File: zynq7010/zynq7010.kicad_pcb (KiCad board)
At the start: 2 copper layers, 50 x 50 mm, 131 parts, among them J1 Conn_02x15_Odd_Even, U1 xc7z010clg400, U2 TPS563200, U3 TPS563200, U4 TPS563200, U5 TPS563200, U6 MT41K256M16HA, U7 MT41K256M16HA

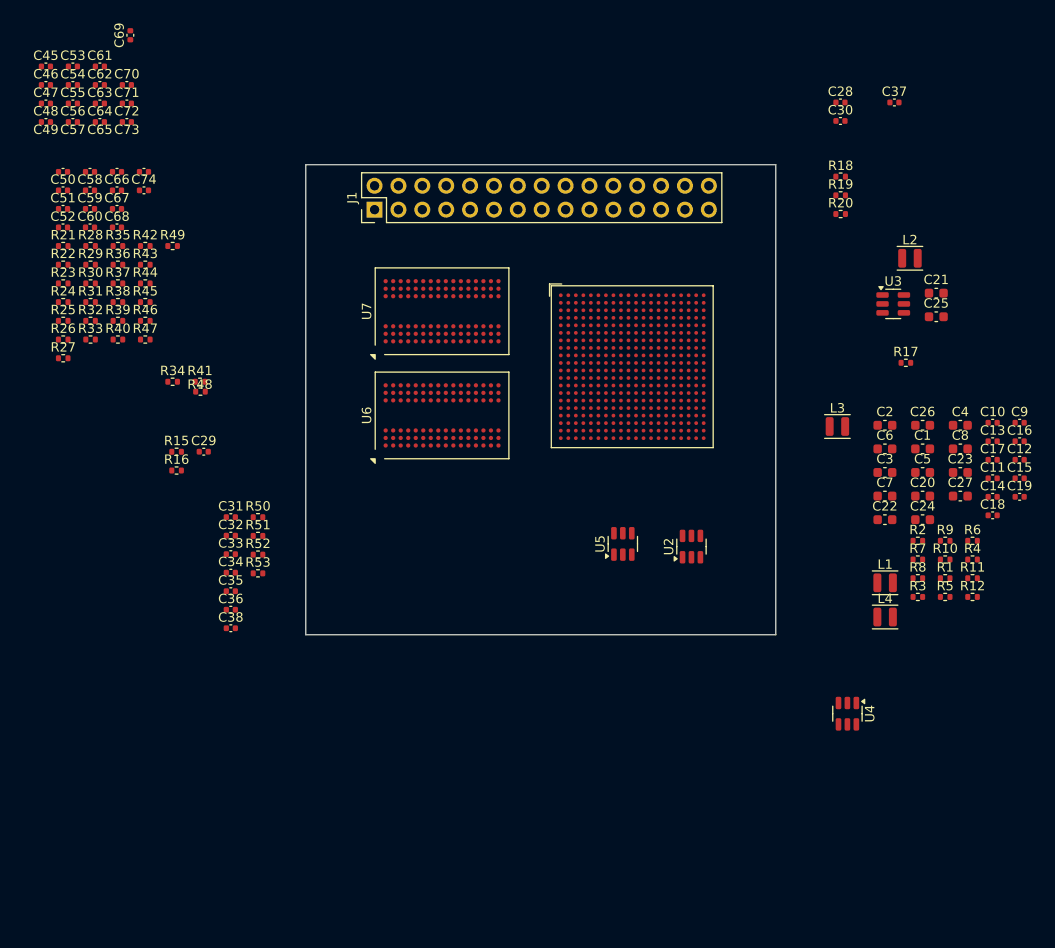
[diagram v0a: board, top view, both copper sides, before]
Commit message: finish dcdc and vtt sch, later do crystal and sd card
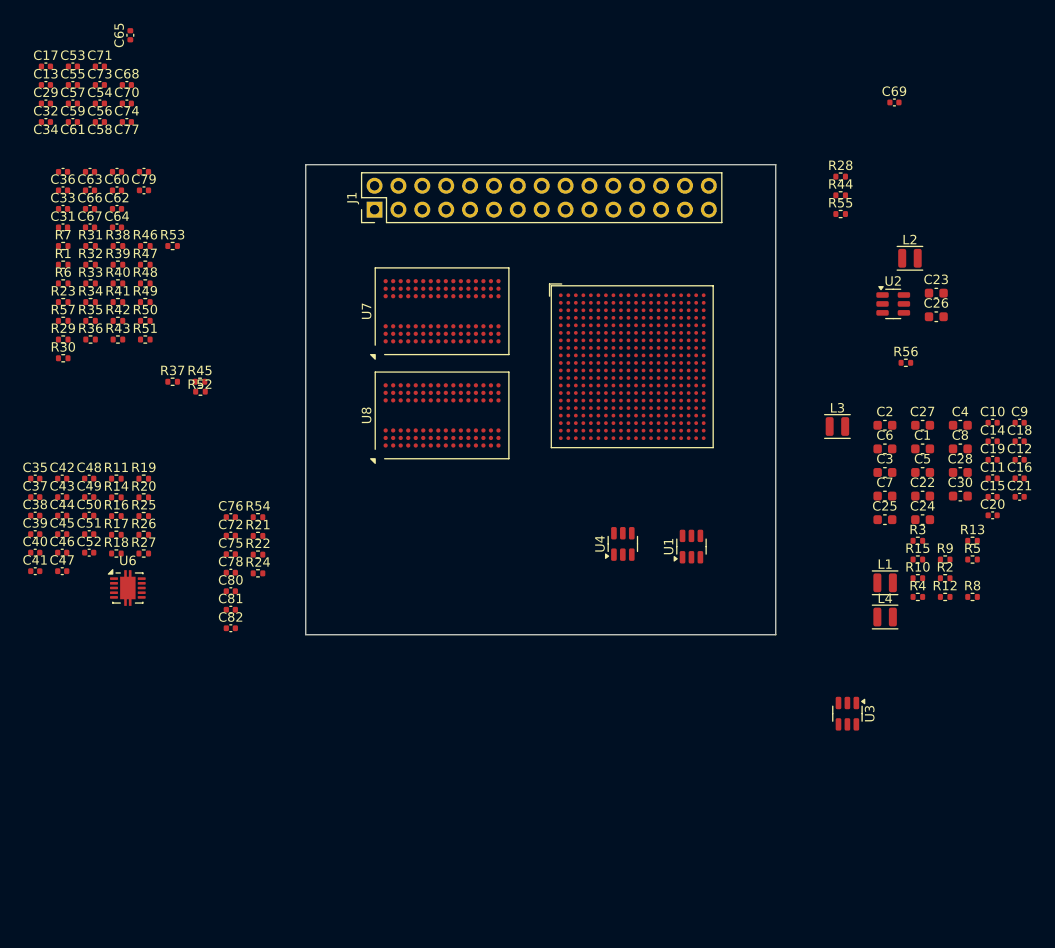
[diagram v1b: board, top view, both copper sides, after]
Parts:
- removed the C28 at (152.9, 49.7)
- removed the C29 at (85.1, 86.9)
- removed the C30 at (152.9, 51.7)
- removed the R15 at (82.2, 86.9)
- removed the R9 at (164.0, 96.3)
- added C35: 4.7uF, Capacitor_SMD:C_0402_1005Metric, F.Cu at (67.2, 89.7)
- added C37: 10uF, Capacitor_SMD:C_0402_1005Metric, F.Cu at (67.2, 91.7)
- added C38: 10uF, Capacitor_SMD:C_0402_1005Metric, F.Cu at (67.2, 93.7)
- added C39: 10uF, Capacitor_SMD:C_0402_1005Metric, F.Cu at (67.2, 95.6)
- added C40: 10uF, Capacitor_SMD:C_0402_1005Metric, F.Cu at (67.2, 97.6)
- added C41: 10uF, Capacitor_SMD:C_0402_1005Metric, F.Cu at (67.2, 99.6)
- added C42: 47uF, Capacitor_SMD:C_0402_1005Metric, F.Cu at (70.1, 89.7)
- added C43: 47uF, Capacitor_SMD:C_0402_1005Metric, F.Cu at (70.1, 91.7)
- added C44: 100nF, Capacitor_SMD:C_0402_1005Metric, F.Cu at (70.1, 93.7)
- added C45: 0.1uF, Capacitor_SMD:C_0402_1005Metric, F.Cu at (70.1, 95.6)
- added C46: 100nF, Capacitor_SMD:C_0402_1005Metric, F.Cu at (70.1, 97.6)
- added C47: 0.1uF, Capacitor_SMD:C_0402_1005Metric, F.Cu at (70.1, 99.6)
- added C48: 10uF, Capacitor_SMD:C_0402_1005Metric, F.Cu at (72.9, 89.7)
- added C49: 0.1uF, Capacitor_SMD:C_0402_1005Metric, F.Cu at (72.9, 91.7)
- added C50: 0.1uF, Capacitor_SMD:C_0402_1005Metric, F.Cu at (72.9, 93.7)
- added C51: 10uF, Capacitor_SMD:C_0402_1005Metric, F.Cu at (72.9, 95.6)
- added C52: 10uF, Capacitor_SMD:C_0402_1005Metric, F.Cu at (72.9, 97.6)
- added R14: 10k, Resistor_SMD:R_0402_1005Metric, F.Cu at (75.8, 91.7)
- added R17: 3.3k, Resistor_SMD:R_0402_1005Metric, F.Cu at (75.8, 95.7)
- added R18: 10k, Resistor_SMD:R_0402_1005Metric, F.Cu at (75.8, 97.7)
- added R19: 10k, Resistor_SMD:R_0402_1005Metric, F.Cu at (78.7, 89.7)
- added R20: 3k, Resistor_SMD:R_0402_1005Metric, F.Cu at (78.7, 91.7)
- added R25: 10k, Resistor_SMD:R_0402_1005Metric, F.Cu at (78.7, 93.7)
- added R26: 10k, Resistor_SMD:R_0402_1005Metric, F.Cu at (78.7, 95.7)
- added R27: 10k, Resistor_SMD:R_0402_1005Metric, F.Cu at (78.7, 97.7)
- added U6: TPS51200DRC, Package_SON:VSON-10-1EP_3x3mm_P0.5mm_EP1.65x2.4mm, F.Cu at (77.1, 101.4)
- R11: value 13.7k -> 7.5k
- R12: renamed from R5; value 13.7k -> 3k
- R15: renamed from R7; value 13.7k -> 10k
- R16: value 1k -> 2k
- moved R11 91.7 mm to (75.8, 89.7)
- moved R16 8.03 mm to (75.8, 93.7)
- renumbered C46 to C13, C13 to C14, C14 to C15, C15 to C16, C45 to C17, C16 to C18, C17 to C19, C18 to C20, C19 to C21, C20 to C22, C21 to C23, C22 to C25, C25 to C26, C26 to C27, C23 to C28, C47 to C29, C27 to C30, C52 to C31, C48 to C32, C51 to C33, C49 to C34, C50 to C36, C63 to C54, C54 to C55, C64 to C56, C55 to C57, C65 to C58, C56 to C59, C66 to C60, C57 to C61, C67 to C62, C58 to C63, C68 to C64, C69 to C65, C59 to C66, C60 to C67, C70 to C68, C37 to C69, C71 to C70, C61 to C71, C32 to C72, C62 to C73, C72 to C74, C33 to C75, C31 to C76, C73 to C77, C34 to C78, C74 to C79, C35 to C80, C36 to C81, C38 to C82, R22 to R1, R8 to R10, R6 to R13, R1 to R2, R51 to R21, R52 to R22, R24 to R23, R53 to R24, R18 to R28, R26 to R29, R2 to R3, R27 to R30, R28 to R31, R29 to R32, R30 to R33, R31 to R34, R32 to R35, R33 to R36, R34 to R37, R35 to R38, R36 to R39, R3 to R4, R37 to R40, R38 to R41, R39 to R42, R40 to R43, R19 to R44, R41 to R45, R42 to R46, R43 to R47, R44 to R48, R45 to R49, R4 to R5, R46 to R50, R47 to R51, R48 to R52, R49 to R53, R50 to R54, R20 to R55, R17 to R56, R25 to R57, R23 to R6, R21 to R7, R12 to R8, R10 to R9, U2 to U1, U3 to U2, U4 to U3, U5 to U4, U1 to U5, U6 to U8
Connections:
- R10 pad 1: Net-(U3-VFB) -> Net-(U2-VFB)
- R11 pad 1: +3V3 -> Net-(U3-VFB)
- R11 pad 2: Net-(U5-VFB) -> Net-(R11-Pad2)
- R15 pad 1: +1V8 -> Net-(U2-VFB)
- R15 pad 2: Net-(U3-VFB) -> Net-(R15-Pad2)
- R16 pad 1: GND -> Net-(R11-Pad2)
- R16 pad 2: VREF_DDR -> +1V5
- R8 pad 1: Net-(U5-VFB) -> Net-(U4-VFB)
- R9 pad 1: Net-(U4-VFB) -> Net-(U3-VFB)
- U2 pad 4: Net-(U3-VFB) -> Net-(U2-VFB)
- U3 pad 4: Net-(U4-VFB) -> Net-(U3-VFB)
- U4 pad 4: Net-(U5-VFB) -> Net-(U4-VFB)

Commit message: done routing between two ddr3
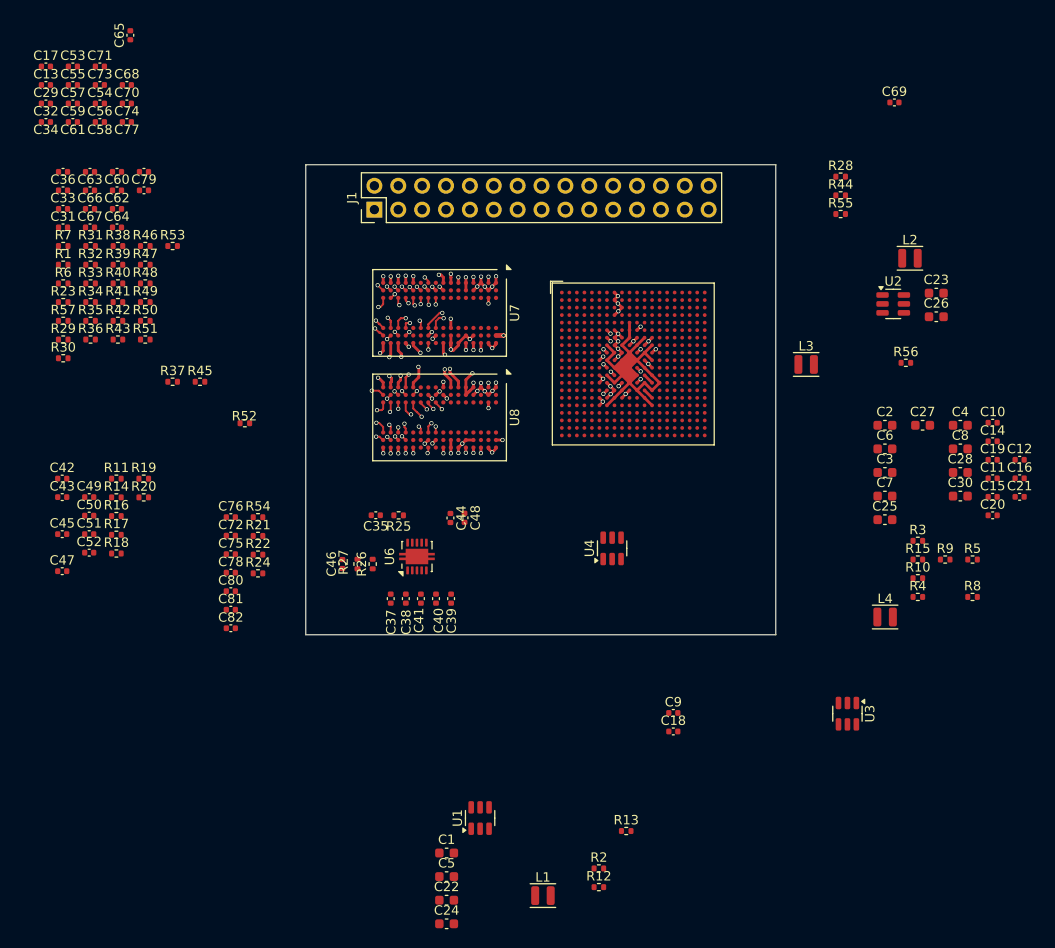
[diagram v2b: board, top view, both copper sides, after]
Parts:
- moved C1 66.4 mm to (111.0, 129.6)
- moved C24 66.4 mm to (111.0, 137.1)
- moved C5 66.4 mm to (111.0, 132.1)
- moved C22 66.4 mm to (111.0, 134.6)
- moved L1 49.3 mm to (121.2, 134.1)
- moved R12 48.1 mm to (127.2, 133.2)
- moved R2 48.1 mm to (127.2, 131.2)
- moved R13 48.1 mm to (130.1, 127.2)
- moved C18 48.1 mm to (135.1, 116.6)
- moved C9 48.1 mm to (135.1, 114.7)
- moved C39 44.8 mm to (111.4, 102.5), turned to -90 degrees
- moved C40 42.9 mm to (109.8, 102.5), turned to -90 degrees
- moved C44 41.3 mm to (111.4, 93.9), turned to -90 degrees
- moved C41 41.1 mm to (108.2, 102.5), turned to -90 degrees
- moved C38 40.4 mm to (106.6, 102.5), turned to 90 degrees
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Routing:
- net GND: track 0.00 -> 87.4 mm, vias 0 -> 38
- net +1V5: track 0.00 -> 31.4 mm, vias 0 -> 37
- net /~{CK}: track 0.00 -> 17.5 mm, vias 0 -> 2
- net /BA2: track 0.00 -> 17.3 mm, vias 0 -> 2
- net /A0: track 0.00 -> 15.8 mm, vias 0 -> 2
- net /A9: track 0.00 -> 15.8 mm, vias 0 -> 2
- net /A1: track 0.00 -> 15.7 mm, vias 0 -> 2
- net /CK: track 0.00 -> 15.6 mm, vias 0 -> 2
- net /A11: track 0.00 -> 15.2 mm, vias 0 -> 2
- net /A13: track 0.00 -> 14.6 mm, vias 0 -> 2
- net /A7: track 0.00 -> 14.5 mm, vias 0 -> 2
- net /A8: track 0.00 -> 14.5 mm, vias 0 -> 2
- net /A14: track 0.00 -> 14.4 mm, vias 0 -> 2
- net /A2: track 0.00 -> 14.4 mm, vias 0 -> 2
- net /~{RAS}: track 0.00 -> 14.3 mm, vias 0 -> 2
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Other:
- copper layers 2 -> 8

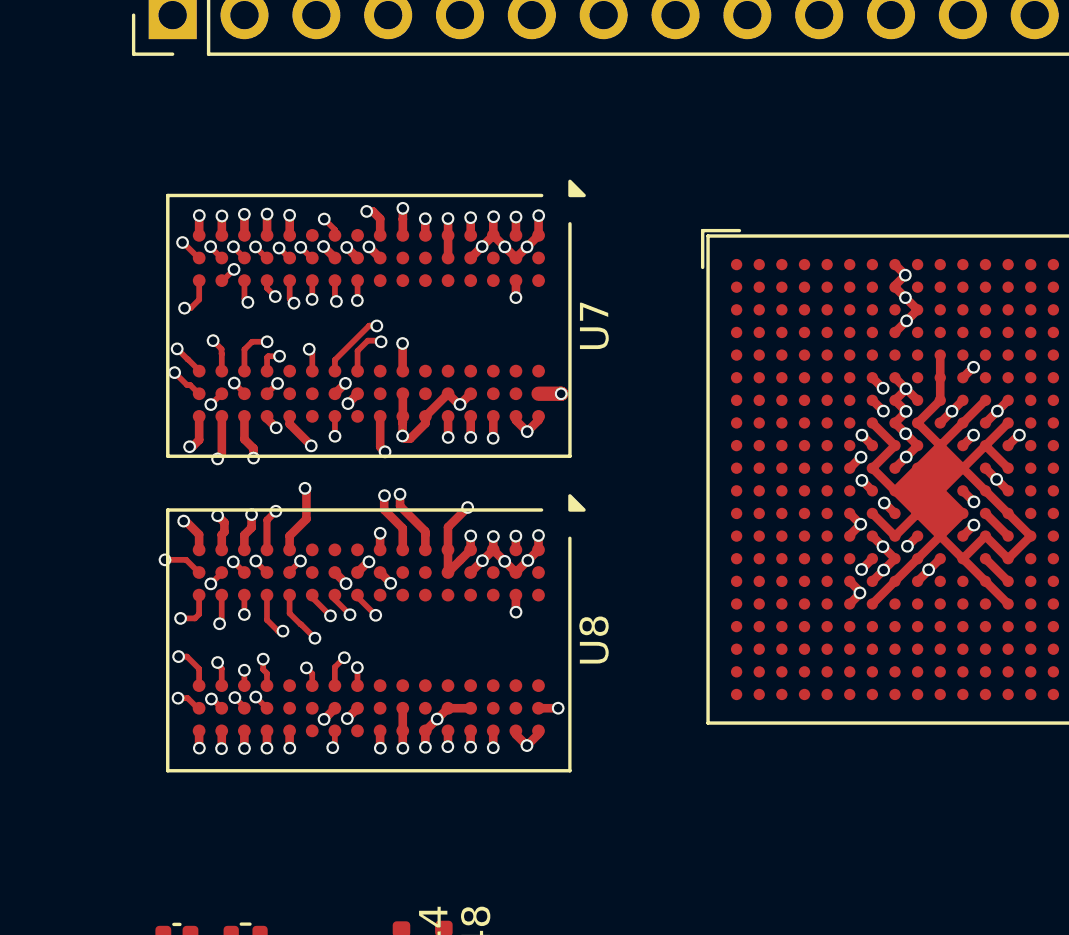
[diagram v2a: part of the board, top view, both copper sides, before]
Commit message: done routing between zynq and two ddr3, not gonna do length matching
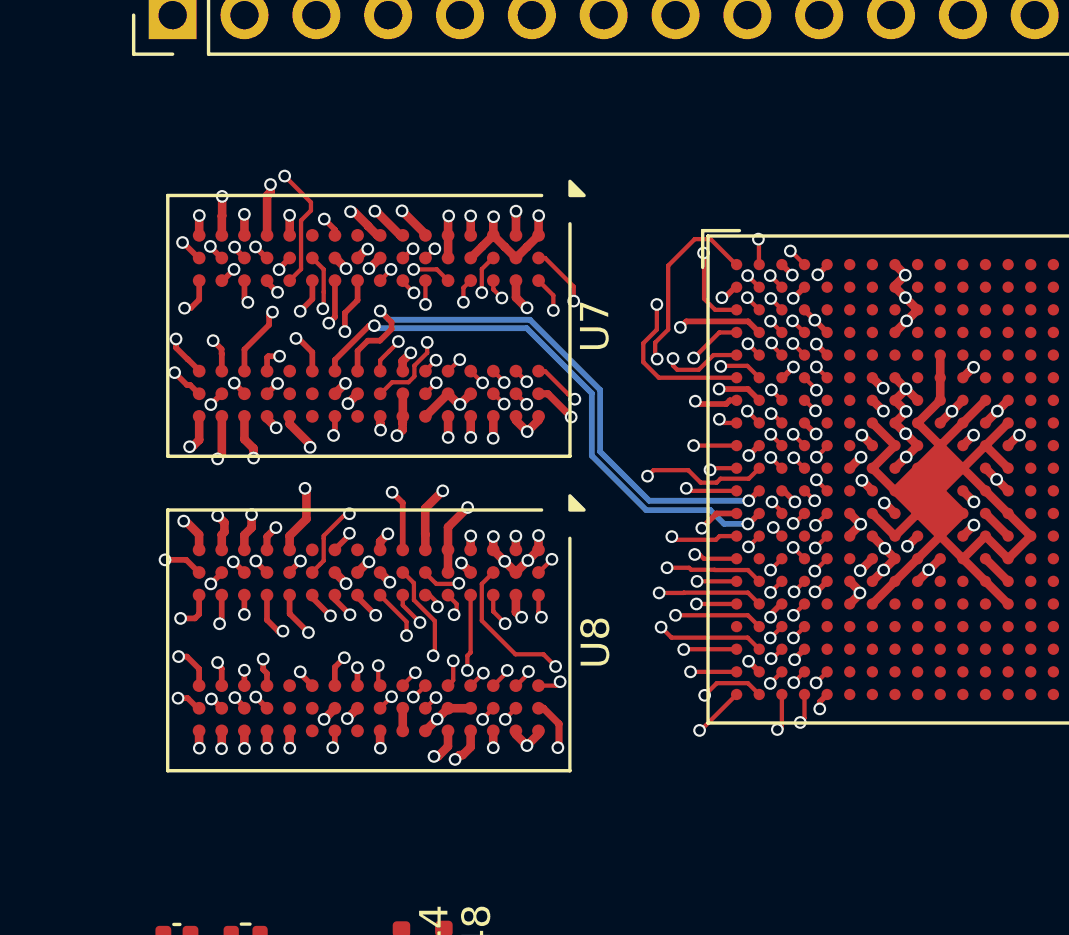
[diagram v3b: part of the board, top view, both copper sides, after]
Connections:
- U7 pad A3: /DQ8 -> /DQ13
- U7 pad C2: /DQ13 -> /DQ9
- U7 pad C3: /DQ9 -> /DQ8
- U7 pad F2: /DQ2 -> /DQ6
- U7 pad F7: /DQ4 -> /DQ7
- U7 pad F8: /DQ0 -> /DQ5
- U7 pad G2: /DQ6 -> /DQ2
- U7 pad H7: /DQ5 -> /DQ0
- U7 pad H8: /DQ7 -> /DQ4
- U8 pad E3: /DQ18 -> /DQ19
- U8 pad F8: /DQ23 -> /DQ21
- U8 pad G2: /DQ17 -> /DQ23
- U8 pad H3: /DQ19 -> /DQ18
- U8 pad H7: /DQ22 -> /DQ17
- U8 pad H8: /DQ21 -> /DQ22
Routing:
- net /A11: track 15.2 -> 64.9 mm, vias 2 -> 3
- net /A8: track 14.5 -> 62.3 mm, vias 2 -> 3
- net /A12: track 14.2 -> 58.7 mm, vias 2 -> 3
- net /ODT: track 0.73 -> 45.1 mm, vias 1 -> 3
- net /A10: track 13.5 -> 56.0 mm, vias 2 -> 3
- net /A14: track 14.4 -> 55.8 mm, vias 2 -> 3
- net /A6: track 14.2 -> 54.0 mm, vias 2 -> 3
- net /~{WE}: track 14.0 -> 53.4 mm, vias 2 -> 3
- net /A4: track 14.0 -> 51.7 mm, vias 2 -> 3
- net /BA2: track 17.3 -> 52.9 mm, vias 2 -> 3
- net /A13: track 14.6 -> 48.4 mm, vias 2 -> 3
- net /~{CS}: track 0.56 -> 34.0 mm, vias 1 -> 3
- net /A7: track 14.5 -> 47.0 mm, vias 2 -> 3
- net /A2: track 14.4 -> 46.8 mm, vias 2 -> 3
- net /A1: track 15.7 -> 48.0 mm, vias 2 -> 3
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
